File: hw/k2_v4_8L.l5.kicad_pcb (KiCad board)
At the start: 8 copper layers, 120 x 46 mm, 46 parts, among them J11 J_EC_HEADER, J12 J_12V_IN, J13 J_SWD, J2 SlimSAS_x8_SFF8654, J3 MCIO_4i_SFF1016, J4 MCIO_4i_SFF1016, J6 J_PWR_CTRL, J9 J_OOB_HEADER, U1 STM32G0B1CBT6, U2 DCDC_12V_3V3, U4 BAT54C, U5 OPTO_LTV356T, U6 DS320PR1601

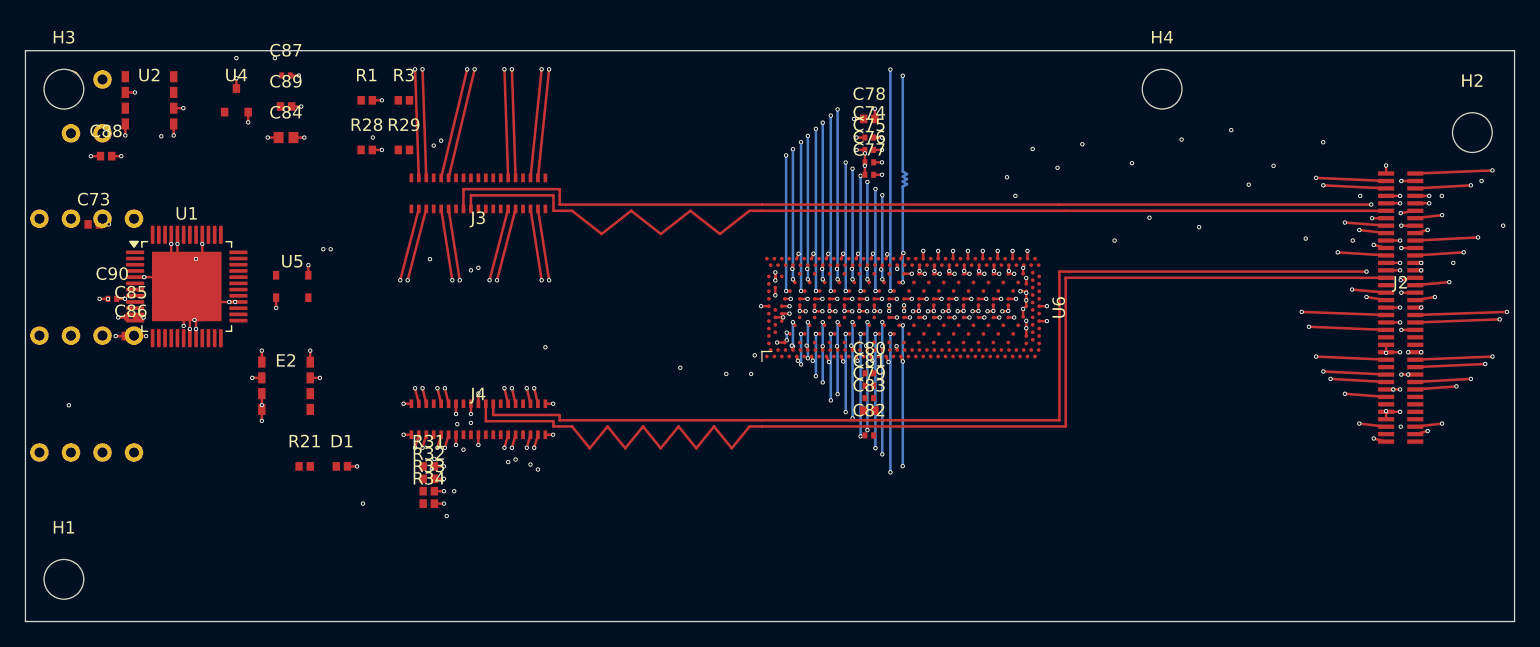
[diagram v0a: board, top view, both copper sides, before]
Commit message: p4(k2): 增量 2 —— IN-5 13 件落板 + C73/C86 移位 + 真源逐 pad 赋网（l5 1b8400a2）；判定 PASS4/FAIL6（pin_map PASS）+ DRC 202/208 + T-1 复跑同一性登记
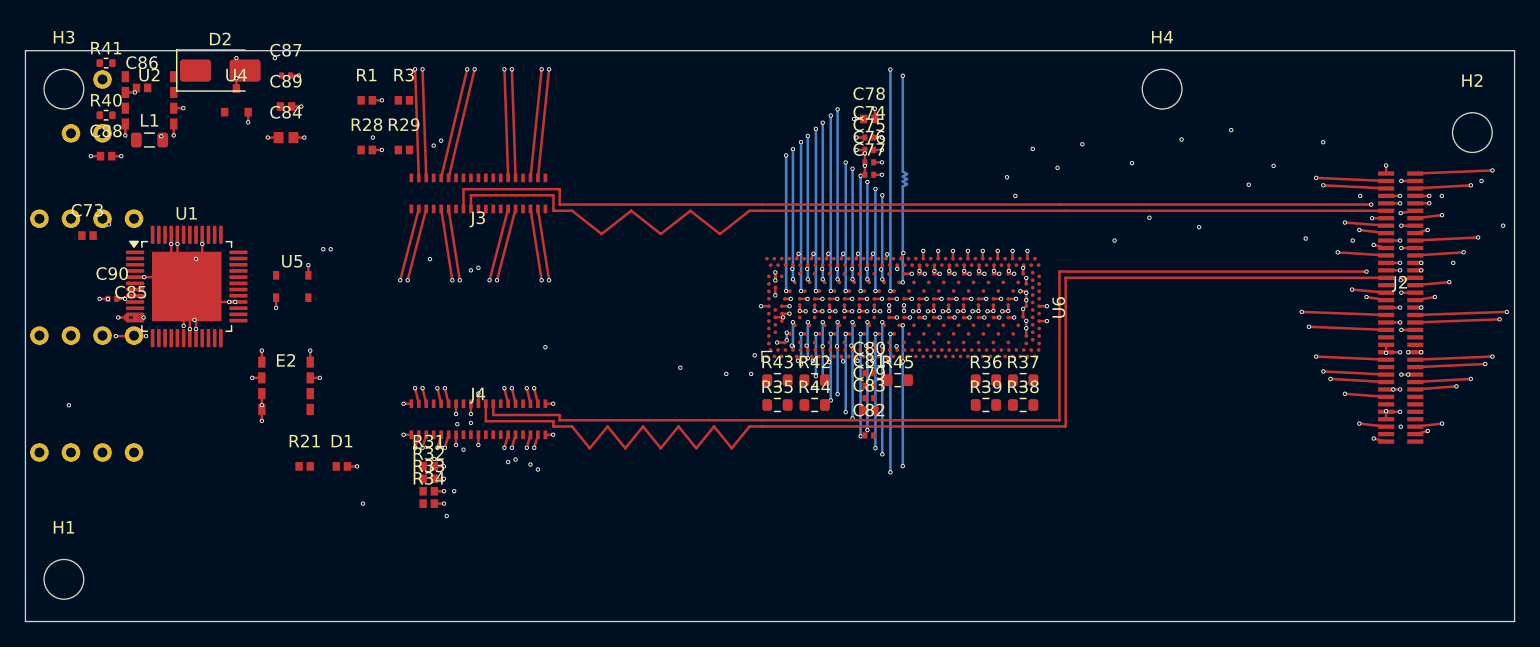
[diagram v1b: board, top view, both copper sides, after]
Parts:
- added D2: SS34, D_SMA, F.Cu at (38.7, 34.6)
- added L1: 10µH, L_0805_2012Metric, F.Cu at (33.0, 40.2)
- added R35: R_6K19, R_0603_1608Metric, F.Cu at (83.6, 61.5)
- added R36: 1K, R_0603_1608Metric, F.Cu at (100.4, 59.5)
- added R37: 1K, R_0603_1608Metric, F.Cu at (103.4, 59.5)
- added R38: R_8K25, R_0603_1608Metric, F.Cu at (103.4, 61.5)
- added R39: 1K, R_0603_1608Metric, F.Cu at (100.4, 61.5)
- added R40: 10K, R_0402_1005Metric, F.Cu at (29.5, 38.2)
- added R41: 5.6k, R_0402_1005Metric, F.Cu at (29.5, 34.0)
- added R42: 1K, R_0603_1608Metric, F.Cu at (86.6, 59.5)
- added R43: 1K, R_0603_1608Metric, F.Cu at (83.6, 59.5)
- added R44: 1K, R_0603_1608Metric, F.Cu at (86.6, 61.5)
- added R45: 1K, R_0603_1608Metric, F.Cu at (93.3, 59.5)
- moved C86 20.0 mm to (32.4, 36.0)
- moved C73 1.03 mm to (28.0, 47.9)
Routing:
- net GND: track 90.6 -> 91.3 mm, vias 169 -> 170
- net MCU_VDD: track 7.55 -> 6.77 mm, vias 16 -> 15
- net SW_U2: vias 0 -> 1
- net P3V3: vias 41 -> 40

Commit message: p4(k2): 增量 3 —— 真源补网（U1 新 pad 7 + 接口件 16 + U6 侧带球 15，gap E 闭合；l5 5c1b0442）；判定 PASS5/FAIL5；登记 U4-D（J-5 结构）+ J-9 口径 + J-1/J-4 九条 ignore 待裁
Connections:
- J11 pad 1: (no net) -> GND
- J11 pad 2: (no net) -> I2C2_SCL
- J11 pad 3: (no net) -> I2C2_SDA
- J11 pad 4: (no net) -> P3V3_AUX
- J12 pad 1: (no net) -> 12V_IN
- J12 pad 2: (no net) -> GND
- J13 pad 1: (no net) -> SWDIO
- J13 pad 2: (no net) -> SWCLK_BOOT0
- J13 pad 3: (no net) -> GND
- J13 pad 4: (no net) -> MCU_VDD
- J6 pad 1: (no net) -> PWR_CTRL_OUT
- J6 pad 2: (no net) -> GND
- J9 pad 1: (no net) -> UART_TX
- J9 pad 2: (no net) -> UART_RX
- J9 pad 3: (no net) -> GND
- J9 pad 4: (no net) -> MCU_VDD
- U1 pad 35: (no net) -> SWDIO
- U1 pad 36: (no net) -> SWCLK_BOOT0
- U1 pad 42: (no net) -> GND
- U1 pad 43: (no net) -> GND
- U1 pad 44: (no net) -> GND
- U1 pad 47: (no net) -> I2C1_SCL
- U1 pad 48: (no net) -> I2C1_SDA
- U6 pad B23: (no net) -> DS320_STRAP_A_ADDR0_7-0
- U6 pad B25: (no net) -> DS320_STRAP_B_ADDR0_7-0
- U6 pad B28: (no net) -> I2C2_SDA
- U6 pad B31: (no net) -> I2C2_SCL
- U6 pad F34: (no net) -> DS320_STRAP_B_ADDR1_7-0
- U6 pad FF24: (no net) -> DS320_STRAP_MODE
- U6 pad FF30: (no net) -> DS320_STRAP_B_ADDR1_15-8
- U6 pad FF33: (no net) -> GND
- U6 pad FF5: (no net) -> DS320_STRAP_A_ADDR0_15-8
- U6 pad FF8: (no net) -> P3V3
- U6 pad FJ28: (no net) -> DS320_STRAP_B_ADDR0_15-8
- U6 pad FJ3: (no net) -> DS320_STRAP_A_ADDR1_15-8
- U6 pad FJ31: (no net) -> GND
- U6 pad FJ6: (no net) -> P3V3
- U6 pad G1: (no net) -> DS320_STRAP_A_ADDR1_7-0
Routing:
- net GND: track 91.3 -> 89.8 mm, vias 170 -> 168
- net MCU_VDD: track 6.77 -> 8.32 mm, vias 15 -> 17
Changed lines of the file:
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@@
 			(layers "*.Cu" "*.Mask")
 			(remove_unused_layers no)
+			(net "GND")
 		)
 		(pad "2" thru_hole circle
@@
 			(layers "*.Cu" "*.Mask")
 			(remove_unused_layers no)
+			(net "I2C2_SCL")
 		)
 		(pad "3" thru_hole circle
@@
 			(layers "*.Cu" "*.Mask")
 			(remove_unused_layers no)
+			(net "I2C2_SDA")
 		)
 		(pad "4" thru_hole circle
@@
 			(layers "*.Cu" "*.Mask")
 			(remove_unused_layers no)
+			(net "P3V3_AUX")
 		)
 		(embedded_fonts no)
@@
 			(layers "*.Cu" "*.Mask")
 			(remove_unused_layers no)
+			(net "12V_IN")
 		)
 		(pad "2" thru_hole circle
@@
 			(layers "*.Cu" "*.Mask")
 			(remove_unused_layers no)
+			(net "GND")
 		)
 		(embedded_fonts no)
@@
 			(layers "*.Cu" "*.Mask")
 			(remove_unused_layers no)
+			(net "SWDIO")
 		)
 		(pad "2" thru_hole circle
@@
 			(layers "*.Cu" "*.Mask")
 			(remove_unused_layers no)
+			(net "SWCLK_BOOT0")
 		)
 		(pad "3" thru_hole circle
@@
 			(layers "*.Cu" "*.Mask")
 			(remove_unused_layers no)
+			(net "GND")
 		)
 		(pad "4" thru_hole circle
@@
 			(layers "*.Cu" "*.Mask")
 			(remove_unused_layers no)
+			(net "MCU_VDD")
 		)
 		(embedded_fonts no)
@@
 			(layers "*.Cu" "*.Mask")
 			(remove_unused_layers no)
+			(net "PWR_CTRL_OUT")
 		)
 		(pad "2" thru_hole circle
@@
 			(layers "*.Cu" "*.Mask")
 			(remove_unused_layers no)
+			(net "GND")
 		)
 		(embedded_fonts no)
@@
 			(layers "*.Cu" "*.Mask")
 			(remove_unused_layers no)
+			(net "UART_TX")
 		)
 		(pad "2" thru_hole circle
@@
 			(layers "*.Cu" "*.Mask")
 			(remove_unused_layers no)
+			(net "UART_RX")
 		)
 		(pad "3" thru_hole circle
@@
 			(layers "*.Cu" "*.Mask")
 			(remove_unused_layers no)
+			(net "GND")
 		)
 		(pad "4" thru_hole circle
@@
 			(layers "*.Cu" "*.Mask")
 			(remove_unused_layers no)
+			(net "MCU_VDD")
 		)
 		(embedded_fonts no)
@@
 			(layers "F.Cu" "F.Mask" "F.Paste")
 			(roundrect_rratio 0.25)
+			(net "SWDIO")
 		)
 		(pad "36" smd roundrect
@@
 			(layers "F.Cu" "F.Mask" "F.Paste")
 			(roundrect_rratio 0.25)
+			(net "SWCLK_BOOT0")
 		)
 		(pad "37" smd roundrect
@@
 			(layers "F.Cu" "F.Mask" "F.Paste")
 			(roundrect_rratio 0.25)
+			(net "GND")
 		)
 		(pad "43" smd roundrect
@@
 			(layers "F.Cu" "F.Mask" "F.Paste")
 			(roundrect_rratio 0.25)
+			(net "GND")
 		)
 		(pad "44" smd roundrect
@@
 			(layers "F.Cu" "F.Mask" "F.Paste")
 			(roundrect_rratio 0.25)
+			(net "GND")
 		)
 		(pad "45" smd roundrect
@@
 			(layers "F.Cu" "F.Mask" "F.Paste")
 			(roundrect_rratio 0.25)
+			(net "I2C1_SCL")
 		)
 		(pad "48" smd roundrect
@@
 			(layers "F.Cu" "F.Mask" "F.Paste")
 			(roundrect_rratio 0.25)
+			(net "I2C1_SDA")
 		)
 		(pad "49" smd rect
@@
 			(size 0.3 0.3)
 			(layers "F.Cu" "F.Mask" "F.Paste")
+			(net "DS320_STRAP_A_ADDR0_7-0")
 		)
 		(pad "B25" smd circle
@@
 			(size 0.3 0.3)
 			(layers "F.Cu" "F.Mask" "F.Paste")
+			(net "DS320_STRAP_B_ADDR0_7-0")
 		)
 		(pad "B28" smd circle
@@
 			(size 0.3 0.3)
 			(layers "F.Cu" "F.Mask" "F.Paste")
+			(net "I2C2_SDA")
 		)
 		(pad "B31" smd circle
@@
 			(size 0.3 0.3)
 			(layers "F.Cu" "F.Mask" "F.Paste")
+			(net "I2C2_SCL")
 		)
 		(pad "BA2" smd circle
@@
 			(size 0.3 0.3)
 			(layers "F.Cu" "F.Mask" "F.Paste")
+			(net "DS320_STRAP_B_ADDR1_7-0")
 		)
 		(pad "FA15" smd circle
@@
 			(size 0.3 0.3)
 			(layers "F.Cu" "F.Mask" "F.Paste")
+			(net "DS320_STRAP_A_ADDR0_15-8")
 		)
 		(pad "FF8" smd circle
@@
 			(size 0.3 0.3)
 			(layers "F.Cu" "F.Mask" "F.Paste")
+			(net "P3V3")
 		)
 		(pad "FF11" smd circle
@@
 			(size 0.3 0.3)
 			(layers "F.Cu" "F.Mask" "F.Paste")
+			(net "DS320_STRAP_MODE")
 		)
 		(pad "FF27" smd circle
@@
 			(size 0.3 0.3)
 			(layers "F.Cu" "F.Mask" "F.Paste")
+			(net "DS320_STRAP_B_ADDR1_15-8")
 		)
 		(pad "FF33" smd circle
@@
 			(size 0.3 0.3)
 			(layers "F.Cu" "F.Mask" "F.Paste")
+			(net "GND")
 		)
 		(pad "FG1" smd circle
@@
 			(size 0.3 0.3)
 			(layers "F.Cu" "F.Mask" "F.Paste")
+			(net "DS320_STRAP_A_ADDR1_15-8")
 		)
 		(pad "FJ6" smd circle
@@
 			(size 0.3 0.3)
 			(layers "F.Cu" "F.Mask" "F.Paste")
+			(net "P3V3")
 		)
 		(pad "FJ9" smd circle
@@
 			(size 0.3 0.3)
 			(layers "F.Cu" "F.Mask" "F.Paste")
+			(net "DS320_STRAP_B_ADDR0_15-8")
 		)
 		(pad "FJ31" smd circle
@@
 			(size 0.3 0.3)
 			(layers "F.Cu" "F.Mask" "F.Paste")
+			(net "GND")
 		)
 		(pad "G1" smd circle
@@
 			(size 0.3 0.3)
 			(layers "F.Cu" "F.Mask" "F.Paste")
+			(net "DS320_STRAP_A_ADDR1_7-0")
 		)
 		(pad "G35" smd circle
@@
 	)
 	(segment
-		(start 31.95 56)
-		(end 32.725 56)
-		(width 0.2)
-		(layer "F.Cu")
-		(net "GND")
-	)
-	(segment
 		(start 132.65 53.7)
 		(end 133.775 53.7)
@@
 	)
 	(segment
-		(start 31.05 56)
-		(end 30.275 56)
-		(width 0.2)
-		(layer "F.Cu")
-		(net "GND")
-	)
-	(segment
 		(start 34.75 49.3)
 		(end 34.75 48.575)
@@
 	)
 	(via
-		(at 32.725 56)
-		(size 0.35)
-		(drill 0.2)
-		(layers "F.Cu" "B.Cu")
-		(net "GND")
-	)
-	(via
 		(at 91.45 37.675)
 		(size 0.35)
@@
 	)
 	(via
-		(at 30.275 56)
-		(size 0.35)
-		(drill 0.2)
-		(layers "F.Cu" "B.Cu")
-		(net "GND")
-	)
-	(via
 		(at 96.825 53)
 		(size 0.35)
@@
 	)
 	(segment
+		(start 31.95 56)
+		(end 32.725 56)
+		(width 0.2)
+		(layer "F.Cu")
+		(net "MCU_VDD")
+	)
+	(segment
 		(start 55.95 66.5)
 		(end 56.725 66.5)
@@
 		(net "MCU_VDD")
 	)
+	(segment
+		(start 31.05 56)
+		(end 30.275 56)
+		(width 0.2)
+		(layer "F.Cu")
+		(net "MCU_VDD")
+	)
 	(via
 		(at 55.75 66.7)
@@
 		(size 0.35)
 		(drill 0.2)
+		(layers "F.Cu" "B.Cu")
+		(net "MCU_VDD")
+	)
+	(via
+		(at 32.725 56)
+		(size 0.35)
+		(drill 0.2)
+		(layers "F.Cu" "B.Cu")
+		(net "MCU_VDD")
+	)
+	(via
+		(at 30.275 56)
+		(size 0.35)
+		(drill 0.2)

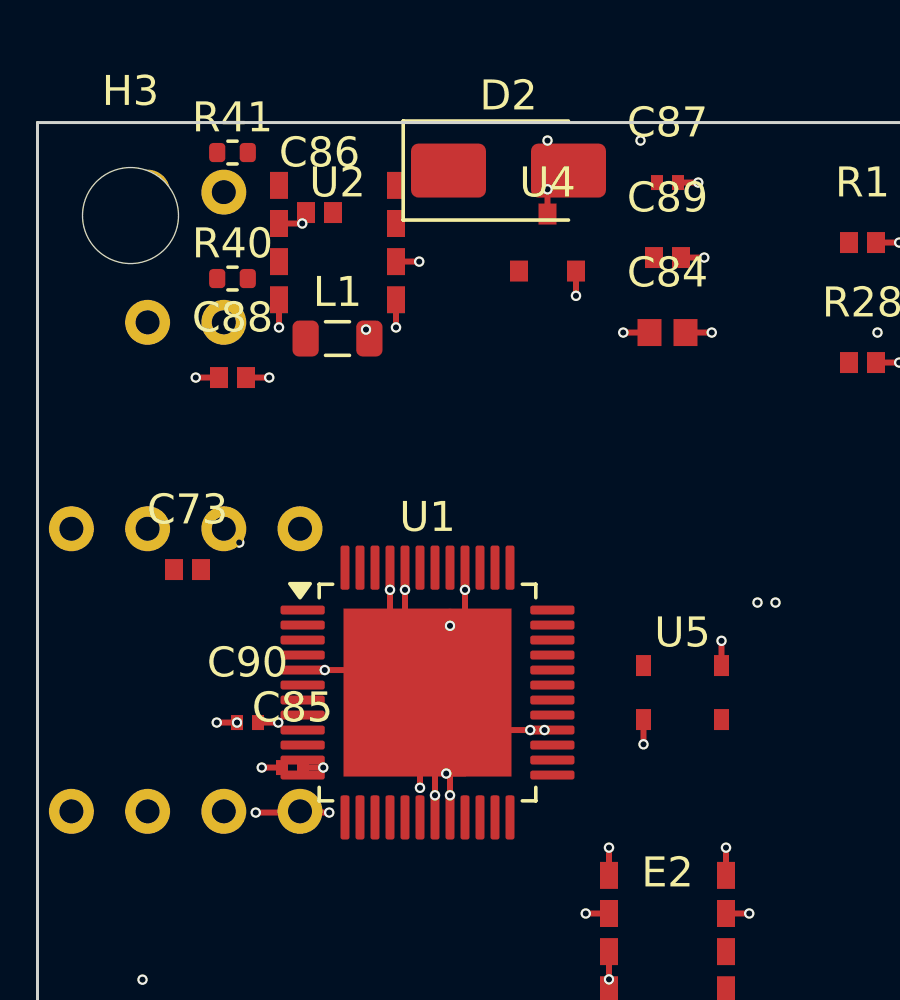
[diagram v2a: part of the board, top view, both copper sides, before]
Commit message: p4(k2): 收敛增量 1（L2 自裁）—— NC 脚网语义归一 + 固定孔 keepout 自门禁 + 参考文字镜像 + 旧铜锚点保持重布 + 丝印离框（l5 eed837f4；DRC 157/236 -> 76/209；判定 PASS5/FAIL5 不变、非45段数不退化）+ SPEC rev-29 留痕 + 状态件 v1
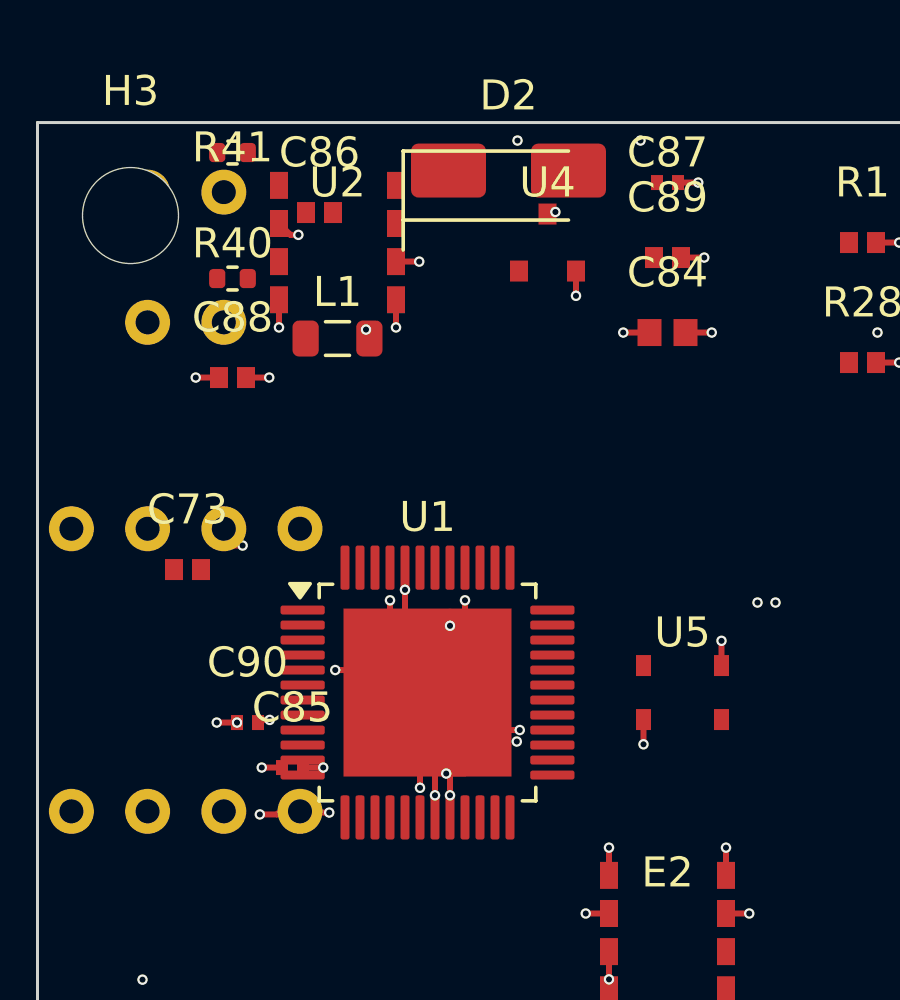
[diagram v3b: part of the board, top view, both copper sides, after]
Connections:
- J2 pad 63: NO_CONNECT -> (no net)
- J2 pad 64: NO_CONNECT -> (no net)
- J3 pad A8: NO_CONNECT -> (no net)
- J3 pad B12: NO_CONNECT -> (no net)
- J3 pad B8: NO_CONNECT -> (no net)
- J3 pad B9: NO_CONNECT -> (no net)
- J4 pad A8: NO_CONNECT -> (no net)
- J4 pad B12: NO_CONNECT -> (no net)
- J4 pad B8: NO_CONNECT -> (no net)
- J4 pad B9: NO_CONNECT -> (no net)
- U1 pad 1: NO_CONNECT -> (no net)
- U1 pad 16: NO_CONNECT -> (no net)
- U1 pad 17: NO_CONNECT -> (no net)
- U1 pad 24: NO_CONNECT -> (no net)
- U1 pad 25: NO_CONNECT -> (no net)
- U1 pad 26: NO_CONNECT -> (no net)
- U1 pad 27: NO_CONNECT -> (no net)
- U1 pad 28: NO_CONNECT -> (no net)
- U1 pad 31: NO_CONNECT -> (no net)
- U1 pad 33: NO_CONNECT -> (no net)
- U1 pad 4: NO_CONNECT -> (no net)
- U1 pad 5: NO_CONNECT -> (no net)
- U1 pad 8: NO_CONNECT -> (no net)
- U1 pad 9: NO_CONNECT -> (no net)
- U2 pad 7: NO_CONNECT -> (no net)
- U2 pad 8: NO_CONNECT -> (no net)
- U4 pad 1: NO_CONNECT -> (no net)
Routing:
- net P3V3_AUX: track 3.00 -> 2.27 mm, vias 12 -> 10
- net MCU_VDD: track 8.32 -> 7.74 mm, vias 17 -> 16
- net P3V3: track 20.9 -> 20.4 mm
- net GND: track 89.8 -> 89.5 mm, vias 168 -> 171

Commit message: p4(k2): 收敛增量 2（L2 自裁）—— 阶段 D GND 平面接入（F.Cu->In1 盲孔 0.20/0.35，沿用既有 std 类，未放松任何 DRC 下限）；未连接 209->196、违规 75（l5 10753591；判定 PASS5/FAIL5 不变、非45不退化）+ SPEC rev-30 留痕 + 状态件 v2
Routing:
- net GND: track 89.5 -> 95.4 mm, vias 171 -> 183

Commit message: p4(k2): 收敛增量 3（L2 自裁）—— GND 平面接入 v2（阶段 E：真盲孔 F.Cu→In1 盘中孔）
- 动因 T-3：v1 阶段 D 的 clear_pt/clear_seg 不分层 ⇒ 把 In2/In5/B.Cu 走线当 F→In1 孔障碍 ⇒ 系统性
  no-legal-slot 115；按层重算后同一几何 139/140 有合法位（133 支在焊盘中心）。⇒ U6/J3 地球主体闭合，
  无需重解 W3 逃逸走廊/PCIe 85Ω/等长。
- 阶段 E（新器 tools/k2_p4_gnd_vias_v1.py）：+129 支真盲孔 F.Cu→In1（0.20/0.35，板内既有唯一类，
  未放松任何 DRC 下限；128 支盘中孔 + 1 组 0/45/90° 同网引线）。
- T-2 实证与更正：本 build pcbnew API 无法置盲孔跨度（恒落 F→B 通孔）⇒ 真盲孔以文件级 (via blind ...) 落；
  增量 2 的 12 支自称 F→In1，经核实为 F→B 通孔（现态合法、DRC 无新增），留痕已更正。
- 实测（同一 DRC 命令）：违规 75 -> 75（类型集不变 9 类，无新增）；未连接 196 -> 72（GND 124 -> 0）；
  判定器 PASS5/FAIL5 集合未变；非 45° 2051 未退化（总段 2535->2537）；两次复跑逐字节同 9efdcc3c8c791d65。
- T-4：本 build pcbnew 同进程加载第二块板 segfault + LoadBoard 依扩展名分发 ⇒ 区域填充另起子进程。
- 边界：未动 l4/设计源板/真源 yaml/criteria/SPEC rev-19..30 原件；未派 WORKER；临时仅 /tmp/opencode。
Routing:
- net GND: track 95.4 -> 95.7 mm, vias 183 -> 312

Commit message: p4(k2): 收敛增量 4（L2 自裁）—— 低速/电源局部闭合（阶段 F1）
- 阶段 F1（新器 tools/k2_p4_ls_local_v1.py）：对 DRC 未连接边取两端铜岛在指定层上最近的可用接点，
  试 ① 同层 F.Cu 0/45/90° 直连 ② 两端铜岛皆在 B.Cu 有铜时 B.Cu 直连；线宽 0.200（= 板内既有
  低速/电源走线口径）；净距 = net class max；板边 0.3；禁 track 禁布区规避；纯增。
- 实测（同一 DRC 命令）：未连接 72 -> 49（+23 条闭合，F.Cu 21 / B.Cu 2）；违规 75 -> 75（类型集不变、
  无新增）；判定器 PASS5/FAIL5 集合未变；非 45° 2051 未增（总段 2537->2579）；复跑两次逐字节同 7f57f9bfd2283193。
- 修过一个真缺陷：F1 首跑引入 1 条 track_dangling（B.Cu 端点选到该铜岛仅 F.Cu 有铜的接点）⇒ 改为按层取接点。
- 声明边界：48 条长距离 / 需在 IC 侧落孔换层的边登记 needs-router（不静默放弃）；已固化 B.Cu 近乎空层
  （39 走线/0 铜区）且西侧插件件 J6/J9/J11/J12/J13 为 PTH（B.Cu 可达）⇒ 后续布线增量有明确落点。
- 边界：未动 l4/设计源板/真源 yaml/criteria/SPEC rev-19..31 原件；未派 WORKER；临时仅 /tmp/opencode。
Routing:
- net P3V3_AUX: track 2.27 -> 35.2 mm
- net GPIO_LED: track 0.00 -> 21.6 mm
- net P3V3: track 20.4 -> 41.1 mm
- net MCU_VDD: track 7.74 -> 22.2 mm
- net SWCLK_BOOT0: track 0.00 -> 13.3 mm
- net I2C1_SCL: track 0.00 -> 11.5 mm
- net I2C1_SDA: track 0.00 -> 11.4 mm
- net NRST: track 0.00 -> 10.1 mm
- net SW_U2: track 0.00 -> 7.71 mm
- net LED_A: track 0.00 -> 2.10 mm
- net FB_U2: track 0.00 -> 1.27 mm
- net 12V_IN: track 2.47 -> 3.52 mm
